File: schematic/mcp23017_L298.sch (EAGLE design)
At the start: 12 parts, among them IC1 MEGA8-P, IC3 MCP23017SP, J1 D8_D13

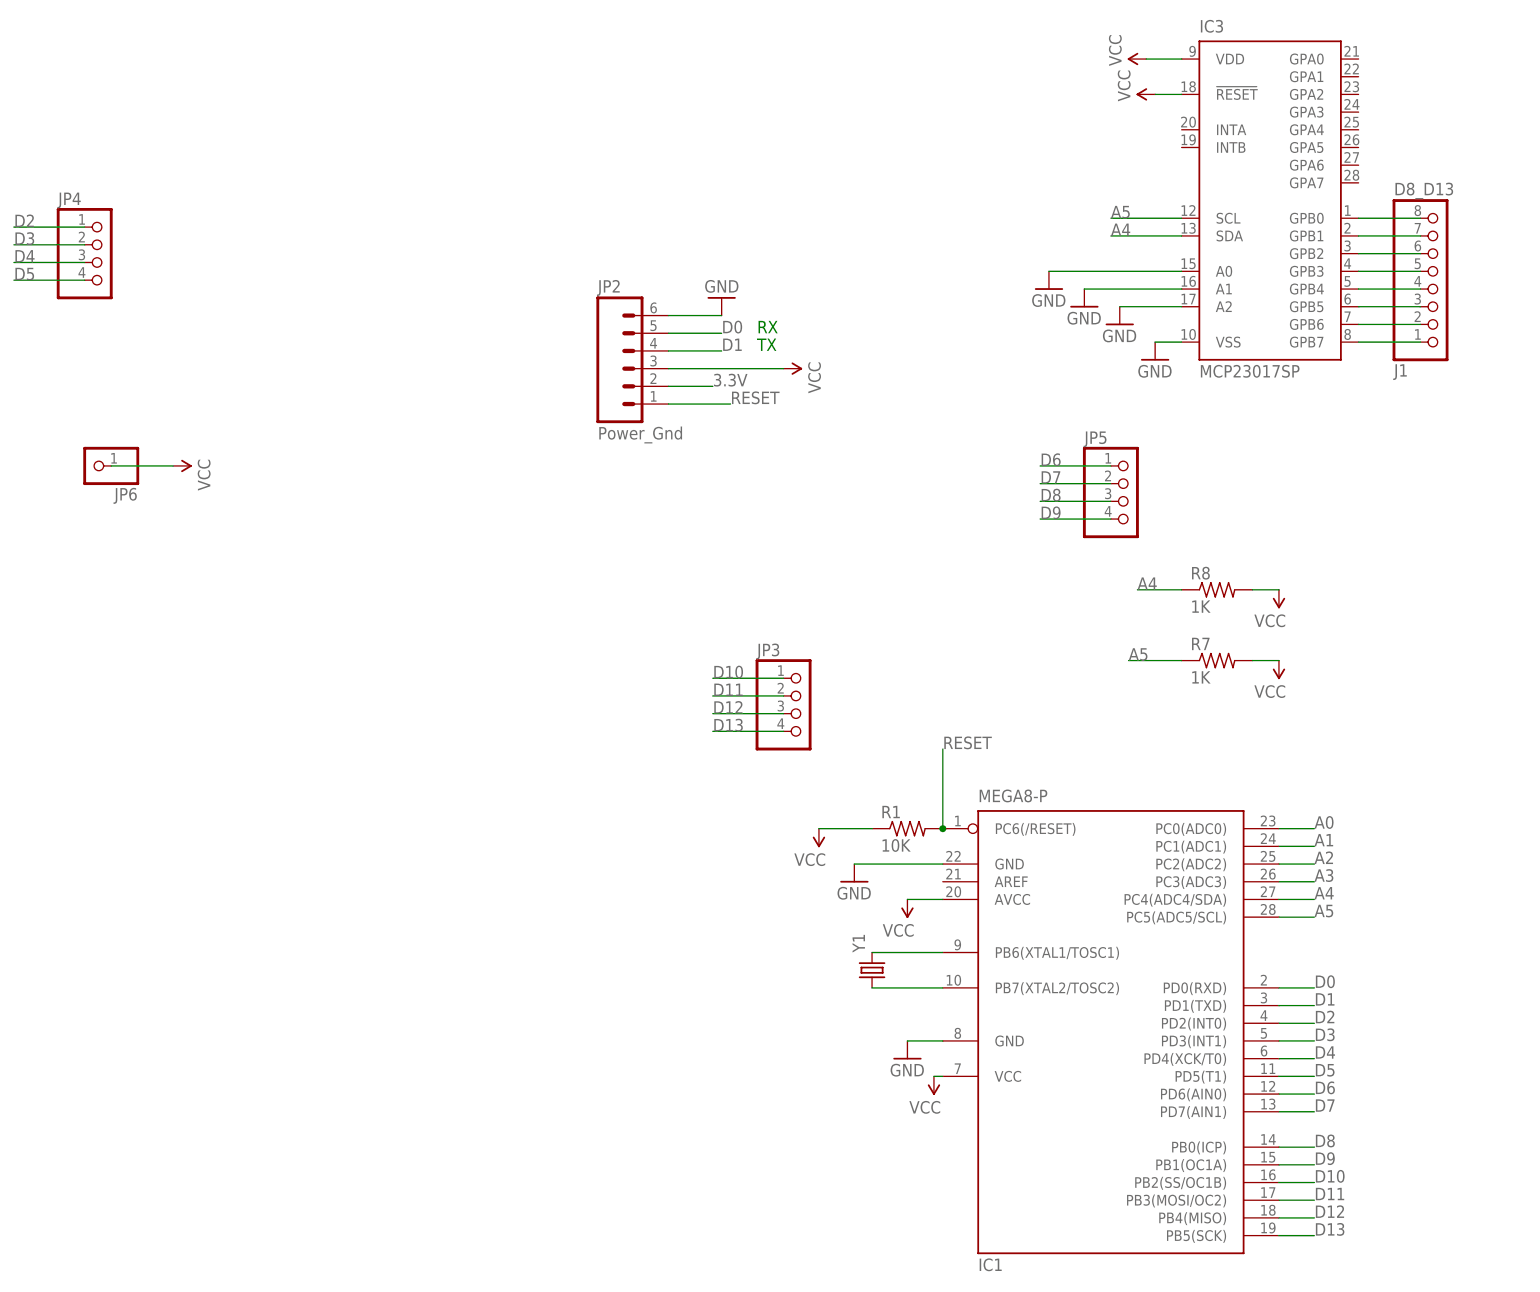
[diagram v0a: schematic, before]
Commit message: v0.05
Ordered updated Schematic from Iteadstudio
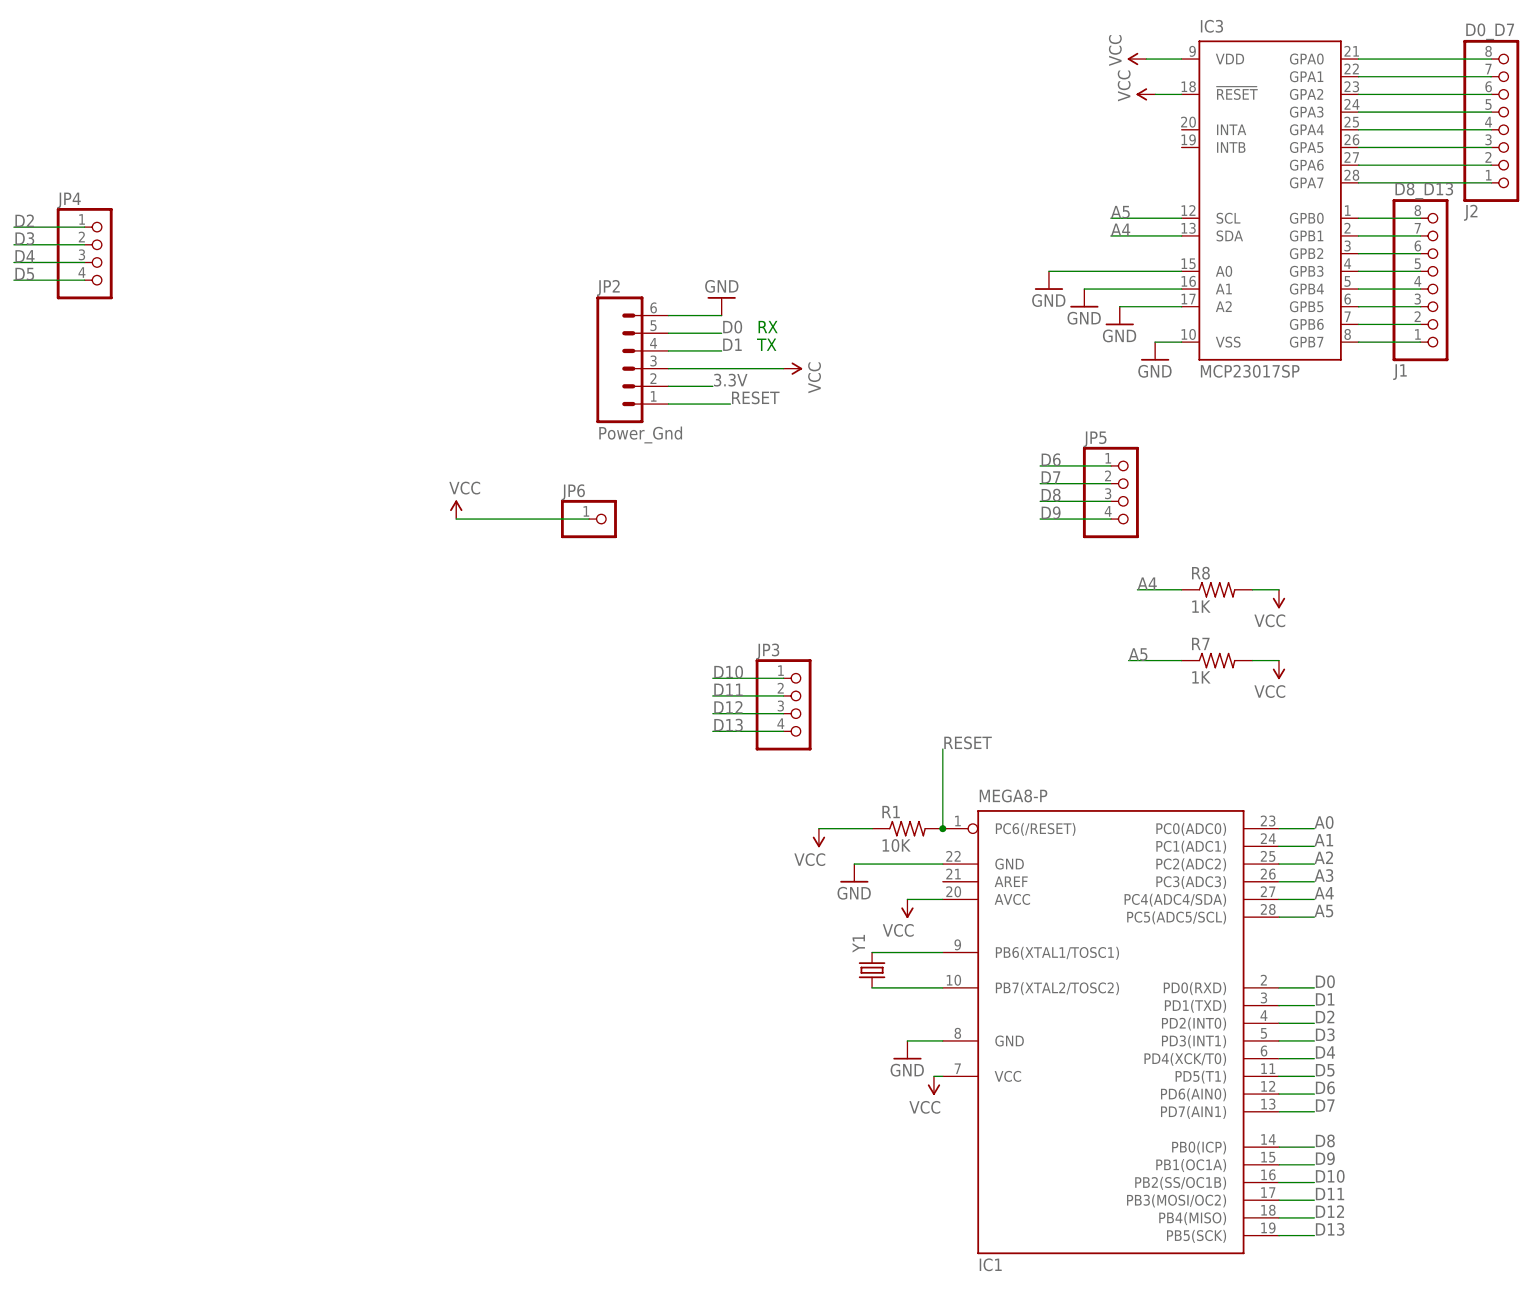
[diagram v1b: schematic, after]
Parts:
- added J2: D0_D7, pinhead:PINHD-1X8
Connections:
- new net N$12: IC3.GPA6, J2.2
- new net N$13: IC3.GPA5, J2.3
- new net N$14: IC3.GPA4, J2.4
- new net N$15: IC3.GPA3, J2.5
- new net N$16: IC3.GPA2, J2.6
- new net N$17: IC3.GPA1, J2.7
- new net N$18: IC3.GPA0, J2.8
- new net N$9: IC3.GPA7, J2.1
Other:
- moved on the sheet: JP6
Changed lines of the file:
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@@
 <part name="P+7" library="SparkFun" deviceset="VCC" device=""/>
 <part name="P+6" library="SparkFun" deviceset="VCC" device=""/>
+<part name="J2" library="pinhead" deviceset="PINHD-1X8" device="" value="D0_D7"/>
 </parts>
 <sheets>
@@
 <instance part="P+16" gate="1" x="162.56" y="38.1" rot="R180"/>
 <instance part="P+17" gate="1" x="162.56" y="27.94" rot="R180"/>
-<instance part="JP6" gate="G$1" x="-7.62" y="55.88" rot="R180"/>
+<instance part="JP6" gate="G$1" x="66.04" y="48.26"/>
 <instance part="J1" gate="A" x="185.42" y="83.82" rot="MR180"/>
 <instance part="IC1" gate="G$1" x="137.16" y="-24.13"/>
@@
 <instance part="GND8" gate="1" x="82.55" y="80.01" rot="R180"/>
 <instance part="P+7" gate="1" x="91.44" y="69.85" rot="R270"/>
-<instance part="P+6" gate="1" x="3.81" y="55.88" rot="R270"/>
+<instance part="P+6" gate="1" x="44.45" y="48.26"/>
+<instance part="J2" gate="A" x="195.58" y="106.68" rot="MR180"/>
 </instances>
 <busses>
@@
 <pinref part="JP6" gate="G$1" pin="1"/>
 <pinref part="P+6" gate="1" pin="VCC"/>
-<wire x1="3.81" y1="55.88" x2="-5.08" y2="55.88" width="0.1524" layer="91"/>
+<wire x1="44.45" y1="48.26" x2="63.5" y2="48.26" width="0.1524" layer="91"/>
 </segment>
 </net>
@@
 </segment>
 </net>
+<net name="N$9" class="0">
+<segment>
+<pinref part="IC3" gate="G$1" pin="GPA7"/>
+<pinref part="J2" gate="A" pin="1"/>
+<wire x1="193.04" y1="96.52" x2="173.99" y2="96.52" width="0.1524" layer="91"/>
+</segment>
+</net>
+<net name="N$12" class="0">
+<segment>
+<pinref part="IC3" gate="G$1" pin="GPA6"/>
+<pinref part="J2" gate="A" pin="2"/>
+<wire x1="193.04" y1="99.06" x2="173.99" y2="99.06" width="0.1524" layer="91"/>
+</segment>
+</net>
+<net name="N$13" class="0">
+<segment>
+<pinref part="IC3" gate="G$1" pin="GPA5"/>
+<pinref part="J2" gate="A" pin="3"/>
+<wire x1="193.04" y1="101.6" x2="173.99" y2="101.6" width="0.1524" layer="91"/>
+</segment>
+</net>
+<net name="N$14" class="0">
+<segment>
+<pinref part="IC3" gate="G$1" pin="GPA4"/>
+<pinref part="J2" gate="A" pin="4"/>
+<wire x1="193.04" y1="104.14" x2="173.99" y2="104.14" width="0.1524" layer="91"/>
+</segment>
+</net>
+<net name="N$15" class="0">
+<segment>
+<pinref part="IC3" gate="G$1" pin="GPA3"/>
+<pinref part="J2" gate="A" pin="5"/>
+<wire x1="193.04" y1="106.68" x2="173.99" y2="106.68" width="0.1524" layer="91"/>
+</segment>
+</net>
+<net name="N$16" class="0">
+<segment>
+<pinref part="IC3" gate="G$1" pin="GPA2"/>
+<pinref part="J2" gate="A" pin="6"/>
+<wire x1="193.04" y1="109.22" x2="173.99" y2="109.22" width="0.1524" layer="91"/>
+</segment>
+</net>
+<net name="N$17" class="0">
+<segment>
+<pinref part="IC3" gate="G$1" pin="GPA1"/>
+<pinref part="J2" gate="A" pin="7"/>
+<wire x1="193.04" y1="111.76" x2="173.99" y2="111.76" width="0.1524" layer="91"/>
+</segment>
+</net>
+<net name="N$18" class="0">
+<segment>
+<pinref part="IC3" gate="G$1" pin="GPA0"/>
+<pinref part="J2" gate="A" pin="8"/>
+<wire x1="193.04" y1="114.3" x2="173.99" y2="114.3" width="0.1524" layer="91"/>
+</segment>
+</net>
